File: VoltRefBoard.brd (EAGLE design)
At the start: 50 x 50 mm, 29 parts, among them J1 BANANA_CONN, J2 BANANA_CONN, J3 BANANA_CONN, J4 BANANA_CONN, J5 BANANA_CONN, U1 MAX6225ACSA+, U2 MAX6250ACSA+

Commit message: Latest commits
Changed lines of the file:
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@@
 <setting verticaltext="up"/>
 </settings>
-<grid distance="0.1" unitdist="mm" unit="mm" style="lines" multiple="1" display="no" altdistance="0.05" altunitdist="mm" altunit="mm"/>
+<grid distance="0.00393700787" unitdist="inch" unit="inch" style="lines" multiple="1" display="no" altdistance="0.00196850394" altunitdist="inch" altunit="inch"/>
 <layers>
 <layer number="1" name="Top" color="4" fill="1" visible="yes" active="yes"/>
@@
 </element>
 <element name="TP1" library="TP_1MM_TH" package="TP_1MM_TH" value="TP_1MM_TH&quot;" x="28.5675" y="4.1925">
-<attribute name="OC_FARNELL" value="unknown" x="28.5675" y="4.1925" size="1.778" layer="27" display="off"/>
-<attribute name="MF" value="" x="28.5675" y="4.1925" size="1.778" layer="27" display="off"/>
-<attribute name="MPN" value="" x="28.5675" y="4.1925" size="1.778" layer="27" display="off"/>
+<attribute name="OC_FARNELL" value="1702006" x="28.5675" y="4.1925" size="1.778" layer="27" display="off"/>
+<attribute name="MF" value="MULTICOMP" x="28.5675" y="4.1925" size="1.778" layer="27" display="off"/>
+<attribute name="MPN" value="TEST-3" x="28.5675" y="4.1925" size="1.778" layer="27" display="off"/>
 </element>
 <element name="TP3" library="TP_1MM_TH" package="TP_1MM_TH" value="TP_1MM_TH&quot;" x="18.4675" y="4.19">
-<attribute name="OC_FARNELL" value="unknown" x="18.4675" y="4.19" size="1.778" layer="27" display="off"/>
-<attribute name="MF" value="" x="18.4675" y="4.19" size="1.778" layer="27" display="off"/>
-<attribute name="MPN" value="" x="18.4675" y="4.19" size="1.778" layer="27" display="off"/>
+<attribute name="OC_FARNELL" value="1702006" x="18.4675" y="4.19" size="1.778" layer="27" display="off"/>
+<attribute name="MF" value="MULTICOMP" x="18.4675" y="4.19" size="1.778" layer="27" display="off"/>
+<attribute name="MPN" value="TEST-3" x="18.4675" y="4.19" size="1.778" layer="27" display="off"/>
 </element>
 <element name="C2" library="rcl" package="C0805" value="2.2uF" x="37.94" y="30.0675" smashed="yes" rot="R90">
@@
 </element>
 <element name="TP2" library="TP_1MM_TH" package="TP_1MM_TH" value="TP_1MM_TH&quot;" x="31.9675" y="4.17">
-<attribute name="OC_FARNELL" value="unknown" x="31.9675" y="4.17" size="1.778" layer="27" display="off"/>
-<attribute name="MF" value="" x="31.9675" y="4.17" size="1.778" layer="27" display="off"/>
-<attribute name="MPN" value="" x="31.9675" y="4.17" size="1.778" layer="27" display="off"/>
+<attribute name="OC_FARNELL" value="1702006" x="31.9675" y="4.17" size="1.778" layer="27" display="off"/>
+<attribute name="MF" value="MULTICOMP" x="31.9675" y="4.17" size="1.778" layer="27" display="off"/>
+<attribute name="MPN" value="TEST-3" x="31.9675" y="4.17" size="1.778" layer="27" display="off"/>
 </element>
 <element name="PAD1" library="wirepad" package="3,81/1,4" value="MOUNT_HOLE" x="46.7225" y="46.6175" smashed="yes">
@@
 </element>
 <element name="LED1" library="P-LCC-2_Shorter" package="P-LCC-2" value="GREEN_LED" x="10.4" y="16.4" smashed="yes">
-<attribute name="MPN" value="" x="1.7" y="30.4" size="1.778" layer="27" display="off"/>
-<attribute name="MF" value="" x="1.7" y="30.4" size="1.778" layer="27" display="off"/>
-<attribute name="OC_FARNELL" value="unknown" x="1.7" y="30.4" size="1.778" layer="27" display="off"/>
+<attribute name="MPN" value="LGT67K-H2K1-24-Z" x="1.7" y="30.4" size="1.778" layer="27" display="off"/>
+<attribute name="MF" value="OSRAM" x="1.7" y="30.4" size="1.778" layer="27" display="off"/>
+<attribute name="OC_FARNELL" value="1226376" x="1.7" y="30.4" size="1.778" layer="27" display="off"/>
 <attribute name="NAME" x="8.46" y="14.595" size="1.27" layer="25" rot="R90"/>
 <attribute name="VALUE" x="14.21" y="14.495" size="1.27" layer="27" rot="R90"/>
@@
 </element>
 <element name="TM1" library="P-LCC-2_Shorter" package="TC33X" value="10k" x="17" y="22.2" rot="R180">
-<attribute name="OC_FARNELL" value="unknown" x="17" y="22.2" size="1.778" layer="27" rot="R180" display="off"/>
-<attribute name="MF" value="" x="17" y="22.2" size="1.778" layer="27" rot="R180" display="off"/>
-<attribute name="MPN" value="" x="17" y="22.2" size="1.778" layer="27" rot="R180" display="off"/>
+<attribute name="OC_FARNELL" value="1141485" x="17" y="22.2" size="1.778" layer="27" rot="R180" display="off"/>
+<attribute name="MF" value="VISHAY SFERNICE" x="17" y="22.2" size="1.778" layer="27" rot="R180" display="off"/>
+<attribute name="MPN" value="TS53YJ103MR10" x="17" y="22.2" size="1.778" layer="27" rot="R180" display="off"/>
 </element>
 <element name="TM2" library="P-LCC-2_Shorter" package="TC33X" value="10k" x="30.3" y="22.3" rot="R180">
-<attribute name="OC_FARNELL" value="unknown" x="30.3" y="22.3" size="1.778" layer="27" rot="R180" display="off"/>
-<attribute name="MF" value="" x="30.3" y="22.3" size="1.778" layer="27" rot="R180" display="off"/>
-<attribute name="MPN" value="" x="30.3" y="22.3" size="1.778" layer="27" rot="R180" display="off"/>
+<attribute name="OC_FARNELL" value="1141485" x="30.3" y="22.3" size="1.778" layer="27" rot="R180" display="off"/>
+<attribute name="MF" value="VISHAY SFERNICE" x="30.3" y="22.3" size="1.778" layer="27" rot="R180" display="off"/>
+<attribute name="MPN" value="TS53YJ103MR10" x="30.3" y="22.3" size="1.778" layer="27" rot="R180" display="off"/>
 </element>
 <element name="F1" library="adafruit" package="1812" value="1.1A" x="10.4" y="29.6" smashed="yes" rot="R90">
@@
 <wire x1="36.8" y1="13.5" x2="36.8" y2="4.18" width="1" layer="1"/>
 <wire x1="31.9675" y1="4.17" x2="36.81" y2="4.17" width="1" layer="1"/>
-<wire x1="36.81" y1="4.17" x2="36.8" y2="4.18" width="0" layer="19" extent="1-1"/>
+<wire x1="36.81" y1="4.17" x2="36.8" y2="4.17" width="0.4064" layer="1"/>
+<wire x1="36.8" y1="4.17" x2="36.8" y2="4.18" width="0.4064" layer="1"/>
 </signal>
 <signal name="V_IN_A">
@@
 <contactref element="S1" pad="6"/>
 <wire x1="19.1" y1="45.6876" x2="19.1" y2="40.9124" width="3.5" layer="1"/>
-<wire x1="19.1" y1="45.7" x2="19.1" y2="40.9" width="3.5" layer="16"/>
+<wire x1="19.1" y1="45.7" x2="19.1" y2="45.6876" width="3.5" layer="16"/>
 <contactref element="J1" pad="P$1"/>
+<wire x1="19.1" y1="45.6876" x2="19.1" y2="40.9" width="3.5" layer="16"/>
 <wire x1="26.6925" y1="45.695" x2="19.1074" y2="45.695" width="3.5" layer="1"/>
 <wire x1="19.1074" y1="45.695" x2="19.1" y2="45.6876" width="3.5" layer="1"/>
-<wire x1="19.1" y1="45.7" x2="19.1074" y2="45.695" width="0" layer="19" extent="1-16"/>
 </signal>
 <signal name="V_IN_B">
@@
 <wire x1="3.9" y1="29.09" x2="3.914" y2="29.276" width="3.5" layer="1"/>
 <wire x1="9.7" y1="40.9124" x2="9.7" y2="45.6876" width="3.5" layer="1"/>
-<wire x1="9.7" y1="45.7" x2="9.7" y2="40.9" width="3.5" layer="16"/>
+<wire x1="9.7" y1="45.7" x2="9.7" y2="45.6876" width="3.5" layer="16"/>
+<wire x1="9.7" y1="45.6876" x2="9.7" y2="40.9" width="3.5" layer="16"/>
 <wire x1="9.7" y1="40.9124" x2="9.7" y2="38.8" width="3.5" layer="1"/>
 <wire x1="9.7" y1="38.8" x2="3.9" y2="33" width="3.5" layer="1"/>
-<wire x1="9.7" y1="45.6876" x2="9.7" y2="45.7" width="0" layer="19" extent="16-16"/>
 </signal>
 <signal name="N$30">
@@
 <contactref element="F1" pad="2"/>
 <wire x1="14.4" y1="45.6876" x2="14.4" y2="40.9124" width="3.5" layer="1"/>
-<wire x1="14.4" y1="45.7" x2="14.4" y2="40.9" width="3.5" layer="16"/>
+<wire x1="14.4" y1="45.7" x2="14.4" y2="45.6876" width="3.5" layer="16"/>
+<wire x1="14.4" y1="45.6876" x2="14.4" y2="40.9" width="3.5" layer="16"/>
 <wire x1="10.4" y1="31.646" x2="10.4" y2="34.6" width="2.5" layer="1"/>
 <wire x1="10.4" y1="34.6" x2="14.3" y2="38.5" width="2.5" layer="1"/>
 <wire x1="14.3" y1="38.5" x2="14.3" y2="40.8124" width="2.5" layer="1"/>
 <wire x1="14.3" y1="40.8124" x2="14.4" y2="40.9124" width="2.5" layer="1"/>
-<wire x1="14.4" y1="45.6876" x2="14.4" y2="45.7" width="0" layer="19" extent="16-16"/>
 </signal>
 <signal name="N$4">

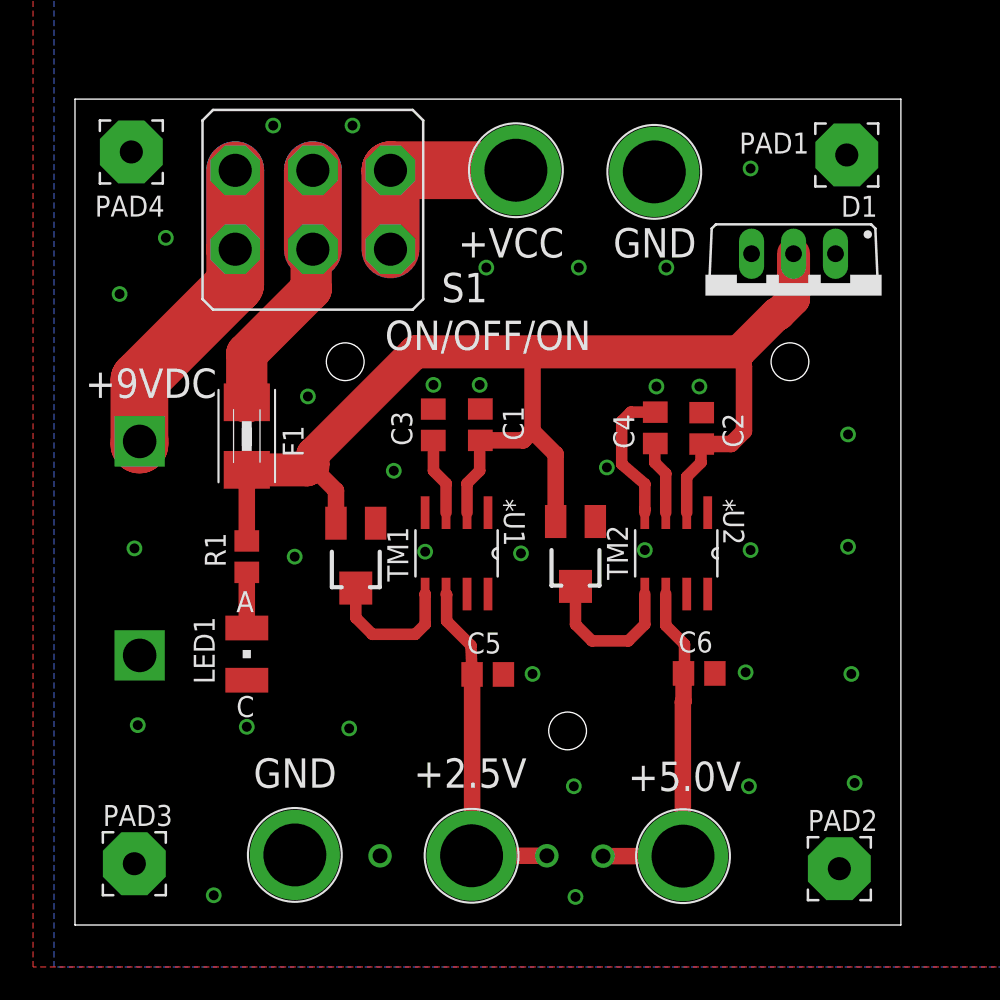
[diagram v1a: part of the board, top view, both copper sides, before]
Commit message: Added the 5x5 pcbs from sick of beige
Added the 5x5 pcbs from sick of beige and added cost down notes to the
schematic to make it cheap to manufacture
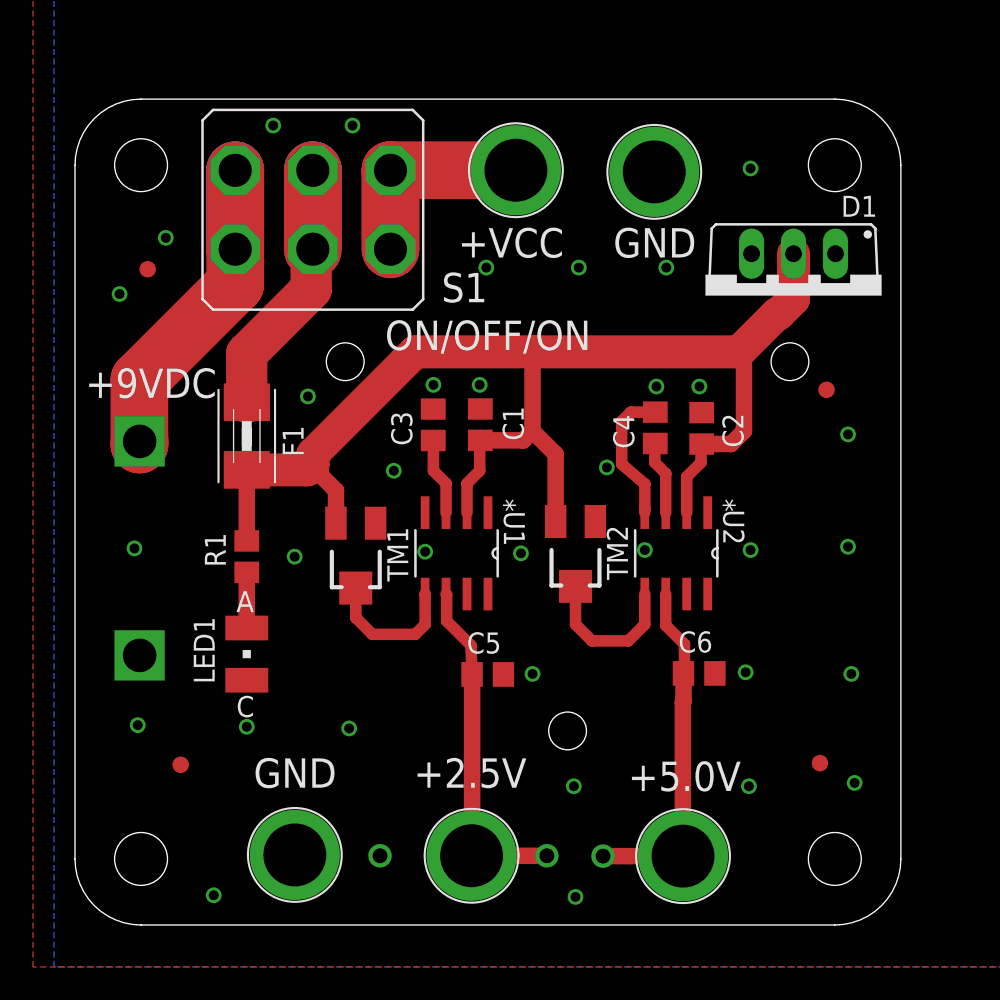
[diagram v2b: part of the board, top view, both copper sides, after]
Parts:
- removed PAD1, PAD2, PAD3, PAD4: MOUNT_HOLE, wirepad:3,81/1,4
- added PCB1: PCB_DP_SQUARE-5X5, dp_devices:DP5050_V1
- added U$1, U$2, U$3, U$4: FIDUCIAL, adafruit:FIDUCIAL_1MM
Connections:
- net GND: no longer PAD1.1, PAD2.1, PAD3.1, PAD4.1
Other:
- outline, holes or cut-outs redrawn
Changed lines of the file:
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@@
 <?xml version="1.0" encoding="utf-8"?>
 <!DOCTYPE eagle SYSTEM "eagle.dtd">
-<eagle version="6.5.0">
+<eagle version="7.5.0">
 <drawing>
 <settings>
@@
 <setting verticaltext="up"/>
 </settings>
-<grid distance="0.00393700787" unitdist="inch" unit="inch" style="lines" multiple="1" display="no" altdistance="0.00196850394" altunitdist="inch" altunit="inch"/>
+<grid distance="0.0999999999" unitdist="mm" unit="mm" style="lines" multiple="1" display="no" altdistance="0.0500000001" altunitdist="mm" altunit="mm"/>
 <layers>
 <layer number="1" name="Top" color="4" fill="1" visible="yes" active="yes"/>
@@
 <layer number="25" name="tNames" color="7" fill="1" visible="yes" active="yes"/>
 <layer number="26" name="bNames" color="7" fill="1" visible="yes" active="yes"/>
-<layer number="27" name="tValues" color="7" fill="1" visible="yes" active="yes"/>
-<layer number="28" name="bValues" color="7" fill="1" visible="yes" active="yes"/>
+<layer number="27" name="tValues" color="7" fill="1" visible="no" active="yes"/>
+<layer number="28" name="bValues" color="7" fill="1" visible="no" active="yes"/>
 <layer number="29" name="tStop" color="7" fill="3" visible="yes" active="yes"/>
 <layer number="30" name="bStop" color="7" fill="6" visible="yes" active="yes"/>
@@
 <layer number="56" name="wert" color="7" fill="1" visible="no" active="no"/>
 <layer number="57" name="tCAD" color="7" fill="1" visible="no" active="no"/>
-<layer number="90" name="Modules" color="5" fill="1" visible="yes" active="yes"/>
+<layer number="90" name="Modules" color="5" fill="1" visible="no" active="no"/>
 <layer number="91" name="Nets" color="2" fill="1" visible="no" active="no"/>
 <layer number="92" name="Busses" color="1" fill="1" visible="no" active="no"/>
@@
 <board>
 <plain>
-<wire x1="0" y1="0" x2="50" y2="0" width="0" layer="20"/>
-<wire x1="50" y1="0" x2="50" y2="50" width="0" layer="20"/>
-<wire x1="50" y1="50" x2="0" y2="50" width="0" layer="20"/>
-<wire x1="0" y1="50" x2="0" y2="0" width="0" layer="20"/>
 <text x="26.4" y="41.3" size="1.778" layer="25" align="center">+VCC</text>
 <text x="36.9" y="9" size="1.778" layer="25" rot="R180" align="center">+5.0V</text>
@@
 <pass name="Default">
 <param name="RoutingGrid" value="50mil"/>
+<param name="AutoGrid" value="1"/>
+<param name="Efforts" value="0"/>
+<param name="TopRouterVariant" value="1"/>
 <param name="tpViaShape" value="round"/>
 <param name="PrefDir.1" value="|"/>
@@
 <attribute name="MPN" value="TEST-3" x="31.9675" y="4.17" size="1.778" layer="27" display="off"/>
 </element>
-<element name="PAD1" library="wirepad" package="3,81/1,4" value="MOUNT_HOLE" x="46.7225" y="46.6175" smashed="yes">
-<attribute name="OC_FARNELL" value="unknown" x="46.7225" y="46.6175" size="1.778" layer="27" display="off"/>
-<attribute name="MF" value="" x="46.7225" y="46.6175" size="1.778" layer="27" display="off"/>
-<attribute name="MPN" value="" x="46.7225" y="46.6175" size="1.778" layer="27" display="off"/>
-<attribute name="NAME" x="40.2175" y="46.7035" size="1.27" layer="25" ratio="10"/>
-<attribute name="VALUE" x="46.7225" y="47.8175" size="0.0254" layer="27"/>
-</element>
-<element name="PAD2" library="wirepad" package="3,81/1,4" value="MOUNT_HOLE" x="46.275" y="3.41">
-<attribute name="OC_FARNELL" value="unknown" x="46.275" y="3.41" size="1.778" layer="27" display="off"/>
-<attribute name="MF" value="" x="46.275" y="3.41" size="1.778" layer="27" display="off"/>
-<attribute name="MPN" value="" x="46.275" y="3.41" size="1.778" layer="27" display="off"/>
-</element>
-<element name="PAD3" library="wirepad" package="3,81/1,4" value="MOUNT_HOLE" x="3.5925" y="3.71">
-<attribute name="OC_FARNELL" value="unknown" x="3.5925" y="3.71" size="1.778" layer="27" display="off"/>
-<attribute name="MF" value="" x="3.5925" y="3.71" size="1.778" layer="27" display="off"/>
-<attribute name="MPN" value="" x="3.5925" y="3.71" size="1.778" layer="27" display="off"/>
-</element>
-<element name="PAD4" library="wirepad" package="3,81/1,4" value="MOUNT_HOLE" x="3.41" y="46.8" smashed="yes">
-<attribute name="OC_FARNELL" value="unknown" x="3.41" y="46.8" size="1.778" layer="27" display="off"/>
-<attribute name="MF" value="" x="3.41" y="46.8" size="1.778" layer="27" display="off"/>
-<attribute name="MPN" value="" x="3.41" y="46.8" size="1.778" layer="27" display="off"/>
-<attribute name="NAME" x="1.205" y="42.886" size="1.27" layer="25" ratio="10"/>
-<attribute name="VALUE" x="3.41" y="48" size="0.0254" layer="27"/>
-</element>
 <element name="LOGO1" library="SparkFun-Aesthetics" package="OSHW-LOGO-L" value="OSHW-LOGOL" x="26.8" y="26.7" rot="MR0">
 <attribute name="OC_FARNELL" value="unknown" x="26.8" y="26.7" size="1.778" layer="28" rot="MR0" display="off"/>
@@
 <attribute name="NAME" x="13.84" y="28.3425" size="1.27" layer="25" rot="R90"/>
 </element>
+<element name="PCB1" library="dp_devices" package="DP5050_V1" value="PCB_DP_SQUARE-5X5" x="25" y="25">
+<attribute name="PCB_SIZE" value="DP5050_V1" x="25" y="25" size="1.778" layer="27" display="off"/>
+</element>
+<element name="U$1" library="adafruit" package="FIDUCIAL_1MM" value="FIDUCIAL" x="6.4" y="9.7"/>
+<element name="U$2" library="adafruit" package="FIDUCIAL_1MM" value="FIDUCIAL" x="45.1" y="9.8"/>
+<element name="U$3" library="adafruit" package="FIDUCIAL_1MM" value="FIDUCIAL" x="45.5" y="32.4"/>
+<element name="U$4" library="adafruit" package="FIDUCIAL_1MM" value="FIDUCIAL" x="4.4" y="39.7"/>
 </elements>
 <signals>
@@
 <contactref element="J2" pad="P$1"/>
 <contactref element="J5" pad="P$1"/>
-<contactref element="PAD4" pad="1"/>
-<contactref element="PAD3" pad="1"/>
-<contactref element="PAD2" pad="1"/>
-<contactref element="PAD1" pad="1"/>
 <contactref element="TP3" pad="P$1"/>
 <polygon width="0.5" layer="1" isolate="0.4064">

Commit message: adding latest updates
adding latest updates
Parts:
- removed BAT1: +9V_BATTERY, BC9VPC_ShortenenSilkScreen:BC9VPC
- removed D1: MBR60H100CTG, diode:TO220ABS
- removed J4, J5: BANANA_CONN, SparkFun-Connectors:BANANA_CONN
- added D2: (no value), adafruit:SOD-323F
- added J6: 1X2-3.5MM, adafruit:1X2-3.5MM
- added TP4: TP_1MM_TH", TP_1MM_TH:TP_1MM_TH
- F1: value 1.1A -> PTC_0805_100MA; device adafruit:1812 -> rcl:R0805
- J1, J2: value BANANA_CONN -> 1X2-3.5MM; device SparkFun-Connectors:BANANA_CONN -> adafruit:1X2-3.5MM
- J3: value BANANA_CONN -> 2060-402; device SparkFun-Connectors:BANANA_CONN -> Wago-2060-402:WAGO_2060-402
- S1: value 5649A -> (none); device Switch_320-938_Corrected:320-938 -> SparkFun-Electromechanical:SWITCH-SPST-SMD-A
- moved J3 48.8 mm to (69.6, 21.6)
- moved J1 41.4 mm to (17.0, 5.40)
- moved J2 40.2 mm to (33.0, 5.40)
- moved F1 8.35 mm to (16.2, 35.6)
- moved U$3 7.52 mm to (46.1, 39.9)
- moved R1 7.45 mm to (13.2, 29.2)
- moved TP2 7.33 mm to (39.2, 2.77)
- moved TP3 7.04 mm to (11.6, 2.79)
- moved LED1 6.67 mm to (13.1, 22.5)
- moved U$4 6.03 mm to (9.00, 43.6)
- moved TP1 5.77 mm to (23.0, 2.79)
- moved S1 4.44 mm to (17.0, 46.9), turned to 0 degrees
- moved C5 2.26 mm to (23.4, 16.8)
- moved C6 1.86 mm to (36.7, 16.7)
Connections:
- removed net V_IN_B: BAT1.V+, S1.1, S1.4
- net +2.5V_REF: now also J1.1; no longer J3.P$1
- net +5.0V_REF: now also J2.1; no longer J4.P$1
- net GND: now also D2.A, J1.2, J2.2, J6.2, TP4.P$1; no longer BAT1.V-, D1.A1, D1.A2, J2.P$1, J5.P$1
- net V_IN_0: no longer S1.5
- net V_IN_1: now also D2.C; no longer D1.C
- net V_IN_A: now also J6.1; no longer J1.P$1, S1.6
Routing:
- net V_IN_B: track 24.0 -> 0.00 mm
- net +2.5V_REF: track 21.0 -> 34.6 mm
- net V_IN_0: track 20.5 -> 8.62 mm
- net V_IN_1: track 80.3 -> 72.0 mm
- net +5.0V_REF: track 21.2 -> 29.5 mm
- net V_IN_A: track 17.2 -> 15.3 mm
- net N$30: track 3.37 -> 4.79 mm
- net GND: vias 34 -> 52
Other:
- board text added: "+VIN"
- board text added: "ON/OFF"
- board text removed: "+9VDC"
- board text removed: "+VCC"
- board text removed: "-=BATTERY HOLDER THIS SIDE=-"
- board text removed: "ON/OFF/ON"

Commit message: minor updates
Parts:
- removed J3: 2060-402, Wago-2060-402:WAGO_2060-402
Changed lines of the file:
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@@
 <text x="27.3" y="7.025" size="1.778" layer="25" rot="R270" align="center">GND</text>
 <text x="11.5" y="7.025" size="1.778" layer="25" rot="R270" align="center">GND</text>
-<wire x1="27.3" y1="12.4" x2="13.8" y2="12.4" width="1.27" layer="46"/>
+<wire x1="26.3" y1="12.4" x2="13.8" y2="12.4" width="1.27" layer="46"/>
 <wire x1="13.8" y1="12.4" x2="9.2" y2="17" width="1.27" layer="46"/>
-<wire x1="31.3" y1="12.5" x2="41.6" y2="12.5" width="1.27" layer="46"/>
+<wire x1="32.5" y1="12.5" x2="41.6" y2="12.5" width="1.27" layer="46"/>
 <wire x1="41.6" y1="12.5" x2="45.1" y2="15.8" width="1.27" layer="46"/>
 <wire x1="45.1" y1="36.2" x2="42.5" y2="38.8" width="1.27" layer="46"/>
@@
 <attribute name="VALUE" x="15.3" y="31.6" size="0.8128" layer="27" font="vector" rot="R90"/>
 </element>
-<element name="J3" library="Wago-2060-402" package="WAGO_2060-402" value="2060-402" x="69.6" y="21.6">
-<attribute name="MPN" value="2060-402/998-404" x="69.6" y="21.6" size="1.778" layer="27" display="off"/>
-<attribute name="OC_NEWARK" value="62T0379 " x="69.6" y="21.6" size="1.778" layer="27" display="off"/>
-<attribute name="PACKAGE" value="SMD-R/A" x="69.6" y="21.6" size="1.778" layer="27" display="off"/>
-<attribute name="SUPPLIER" value="WAGO" x="69.6" y="21.6" size="1.778" layer="27" display="off"/>
-<attribute name="OC_FARNELL" value="2102477 " x="69.6" y="21.6" size="1.778" layer="27" display="off"/>
-</element>
 </elements>
